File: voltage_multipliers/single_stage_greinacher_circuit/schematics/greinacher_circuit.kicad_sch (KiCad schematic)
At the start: 24 parts

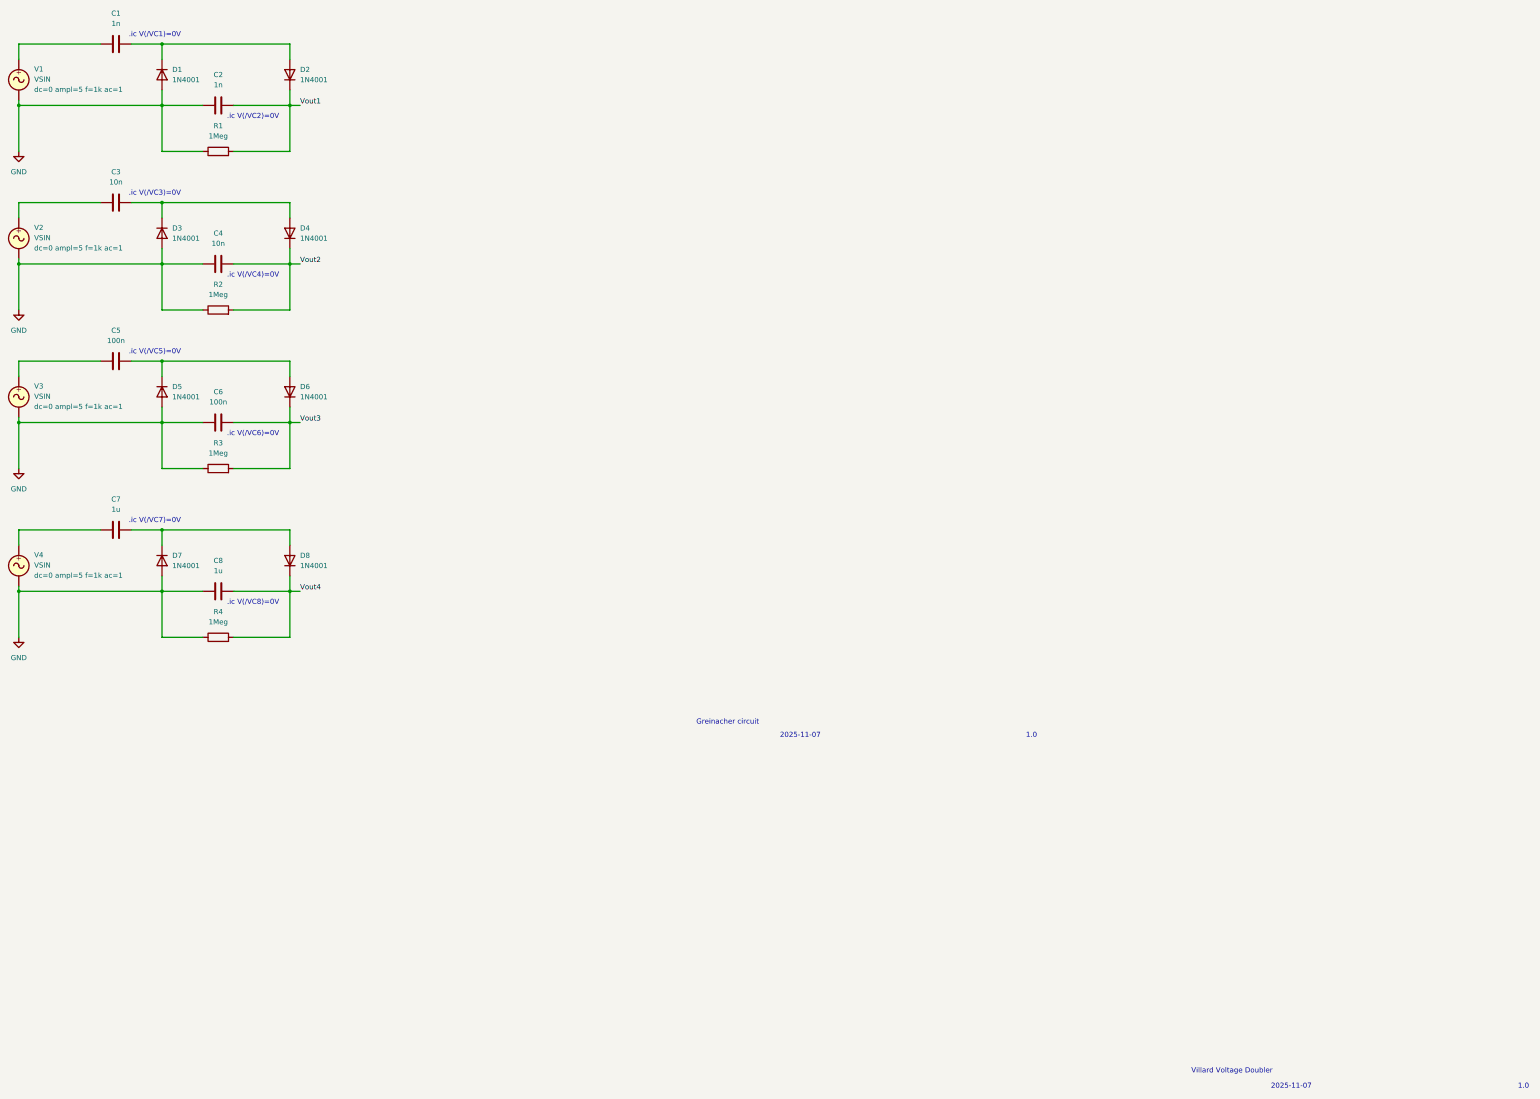
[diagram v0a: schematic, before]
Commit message: feat: Update Greinacher circuit schematics and README
Simplifies the Greinacher circuit schematics for better clarity and
updates the README with additional explanations and usage instructions.

Breaking changes: None

Resolves: None
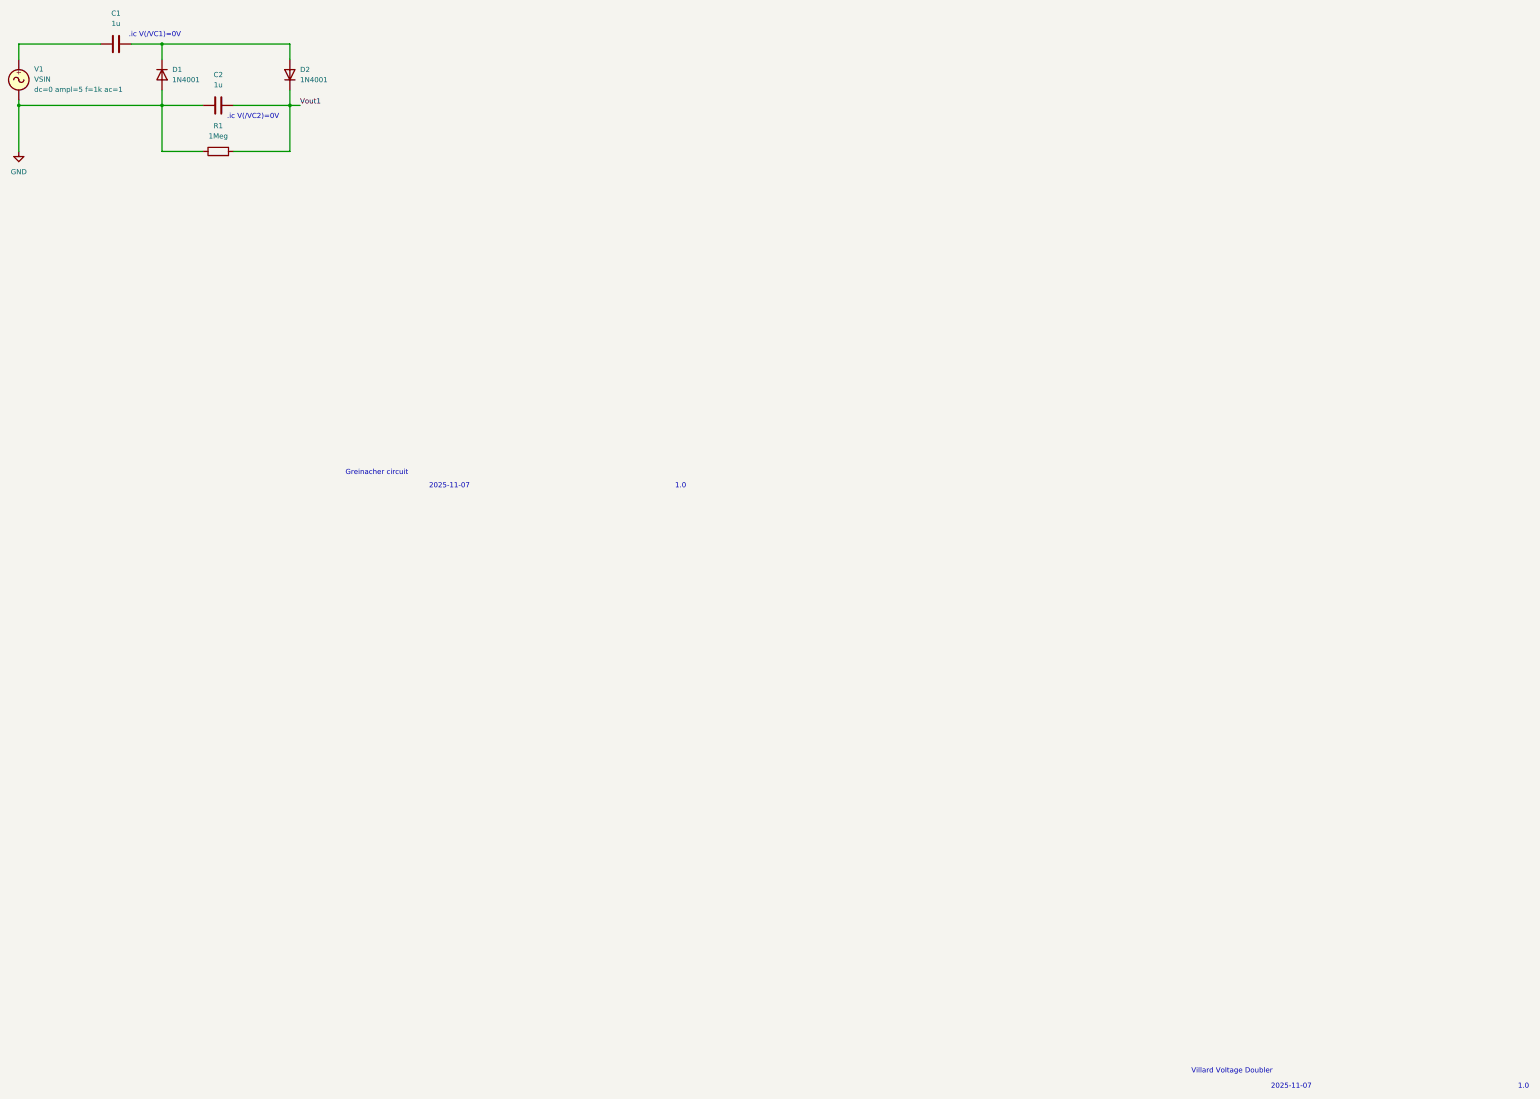
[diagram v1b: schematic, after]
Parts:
- removed C3, C4: 10n, symbol Device:C
- removed C5, C6: 100n, symbol Device:C
- removed C7, C8: 1u, symbol Device:C
- removed D3, D4, D5, D6, D7, D8: 1N4001, Diode_THT:D_DO-41_SOD81_P10.16mm_Horizontal, symbol Diode:1N4001
- removed R2, R3, R4: 1Meg, symbol Device:R
- removed V2, V3, V4: VSIN, symbol Simulation_SPICE:VSIN
- C1, C2: value 1n -> 1u
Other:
- note removed: ".ic V(/VC3)=0V"
- note removed: ".ic V(/VC4)=0V"
- note removed: ".ic V(/VC5)=0V"
- note removed: ".ic V(/VC6)=0V"
- note removed: ".ic V(/VC7)=0V"
- note removed: ".ic V(/VC8)=0V"
